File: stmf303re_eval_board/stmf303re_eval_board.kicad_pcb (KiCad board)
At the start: 2 copper layers, 44.2 x 39.4 mm, 31 parts, among them J1 Conn_01x04_Male, J2 USB_B_Micro, J3 Conn_01x16, J4 Conn_01x16, SW1 SW_DPST_x2, U1 STM32F303RETx, U2 XC6206PxxxMR, Y1 8MHz

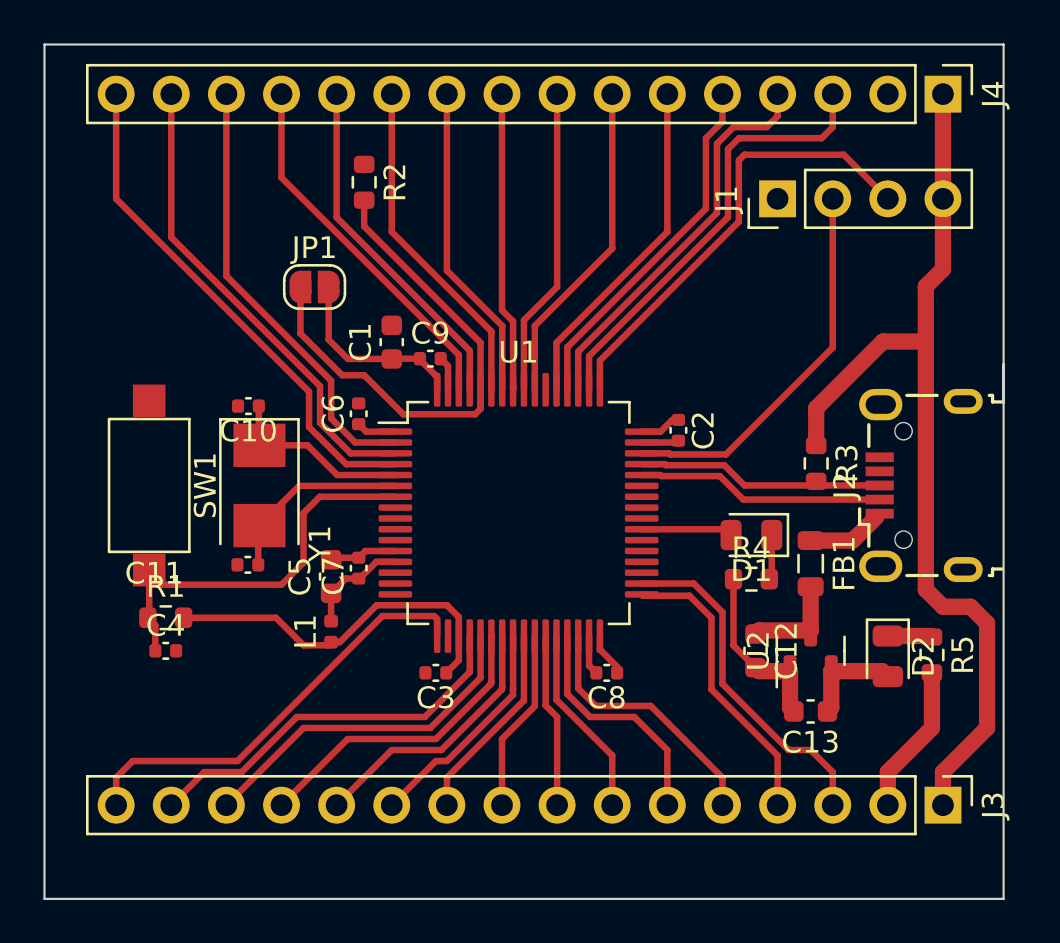
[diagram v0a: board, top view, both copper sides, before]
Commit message: usb, traces fixed
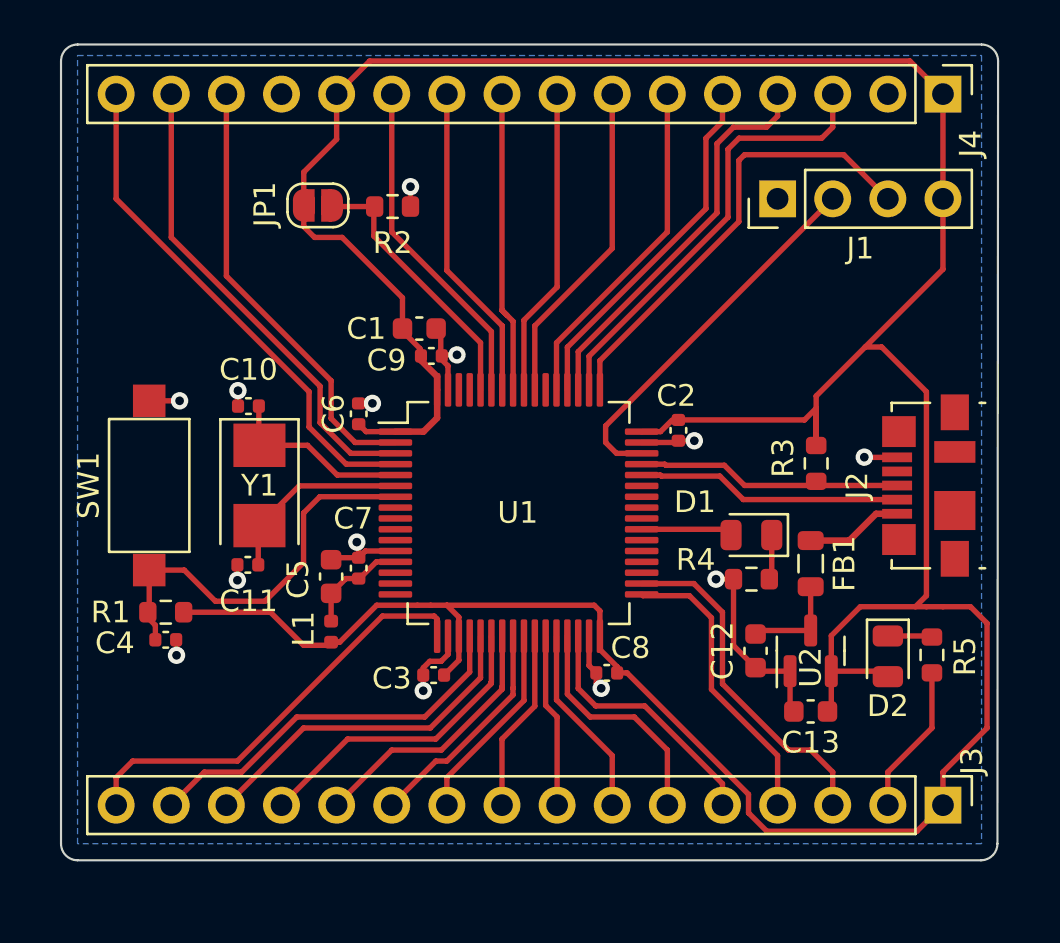
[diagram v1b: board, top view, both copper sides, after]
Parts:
- J2: footprint Connector_USB:USB_Micro-B_Wuerth_629105150521 -> Connector_USB:USB_Micro-B_Molex_47346-0001
- moved JP1 3.76 mm to (142.4, 65.8), turned to 180 degrees
- moved R2 1.72 mm to (145.8, 65.9), turned to 180 degrees
- moved C1 1.42 mm to (147.1, 71.5), turned to 0 degrees
- moved C4 0.51 mm to (135.4, 85.9)
- moved J2 0.36 mm to (170.5, 78.7)
- moved R1 0.25 mm to (135.4, 84.6)
- moved C3 0.14 mm to (147.7, 87.5)
- moved C9 0.14 mm to (147.6, 72.8)
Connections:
- J4 pad 12: PB8 -> +3.3V
- J4 pad 13: PB9 -> GND
- U1 pad 61: PB8 -> unconnected-(U1-Pad61)
- U1 pad 62: PB9 -> unconnected-(U1-Pad62)
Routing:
- net +3.3V: track 80.1 -> 164.7 mm
- net PB9: track 17.0 -> 0.00 mm
- net PB8: track 16.2 -> 0.00 mm
- net GND: track 23.7 -> 38.5 mm, vias 0 -> 13
- net Net-(JP1-Pad1): track 24.8 -> 12.5 mm
- net +5V: track 3.48 -> 4.49 mm
- net USB_D+: track 11.4 -> 12.2 mm
- net USB_D-: track 11.4 -> 12.2 mm
- added copper zone on B.Cu, net GND
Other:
- board size 44.2 x 39.4 mm -> 43.2 x 37.6 mm

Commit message: traces update
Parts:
- J3, J4: footprint Connector_PinHeader_2.54mm:PinHeader_1x16_P2.54mm_Vertical -> Connector_PinSocket_2.54mm:PinSocket_1x16_P2.54mm_Vertical
- Y1: footprint Crystal:Crystal_SMD_5032-2Pin_5.0x3.2mm -> Crystal:Crystal_SMD_0603-2Pin_6.0x3.5mm
- moved C2 0.33 mm to (158.9, 76.5)
- moved C10 0.30 mm to (139.2, 74.8)
- moved C11 0.29 mm to (139.2, 82.7)
- moved C8 0.21 mm to (155.5, 87.3)
- moved C6 0.13 mm to (144.4, 75.4)
- moved R3 0.11 mm to (165.3, 77.6)
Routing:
- net +3.3V: track 164.7 -> 163.0 mm
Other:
- board text added: "+"
- board text added: "-"
- board text added: "SWCLK"
- board text added: "SWDIO"
